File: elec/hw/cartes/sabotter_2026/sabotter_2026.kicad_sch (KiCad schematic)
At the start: 0 parts

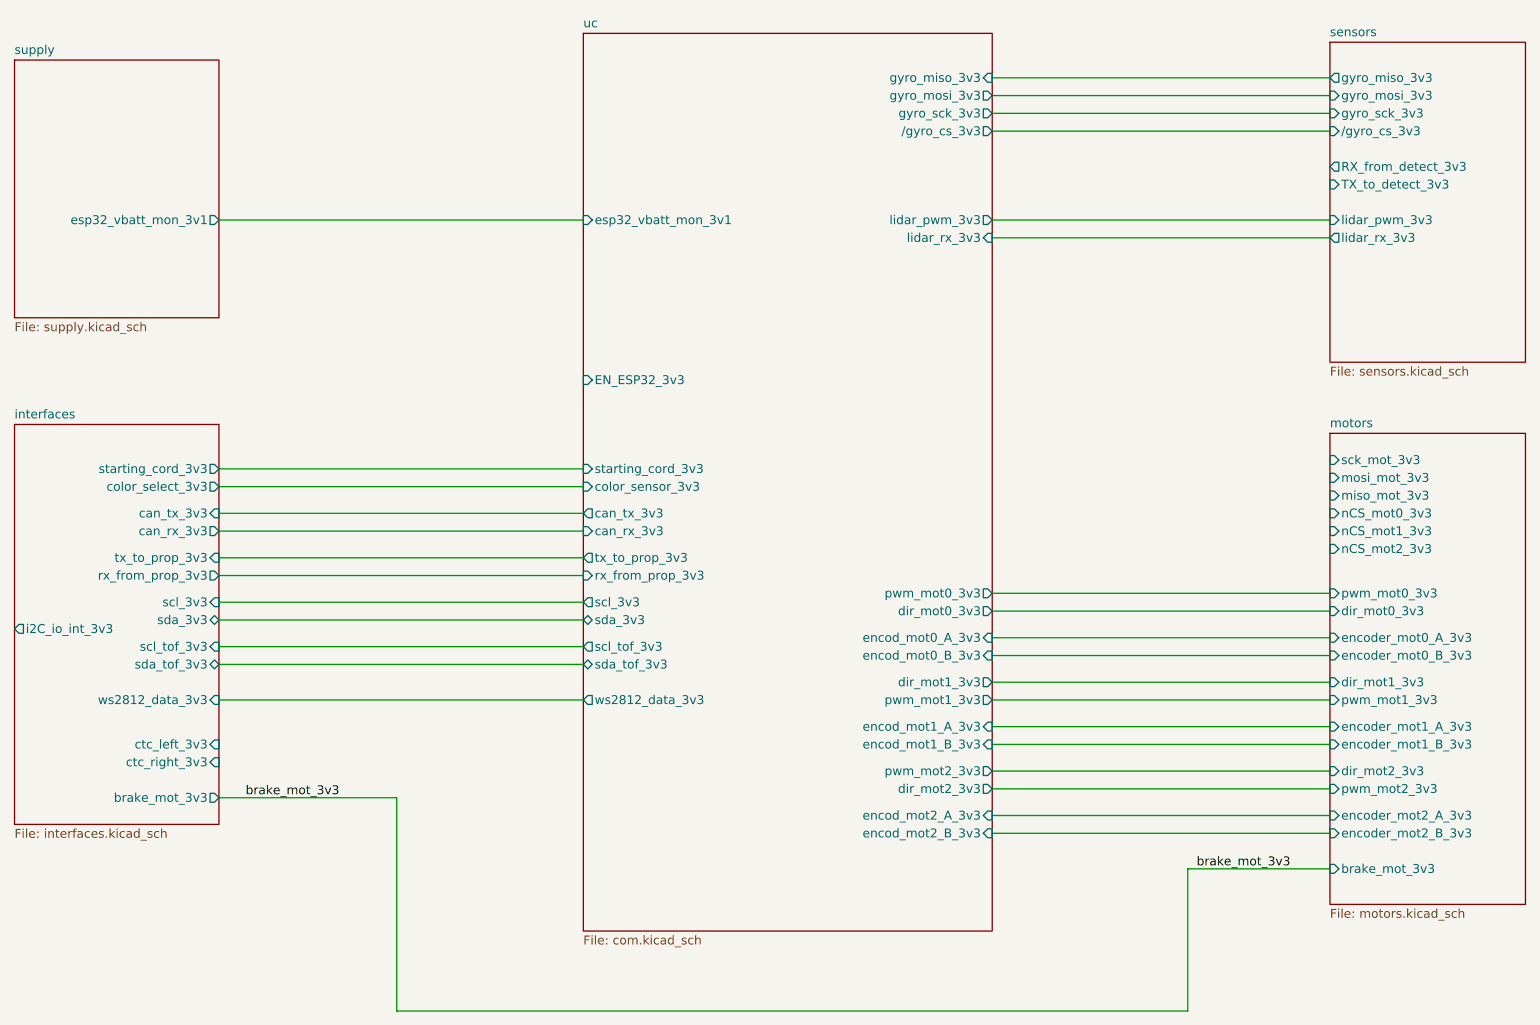
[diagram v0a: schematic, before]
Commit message: switchs added to motor ribbon cable
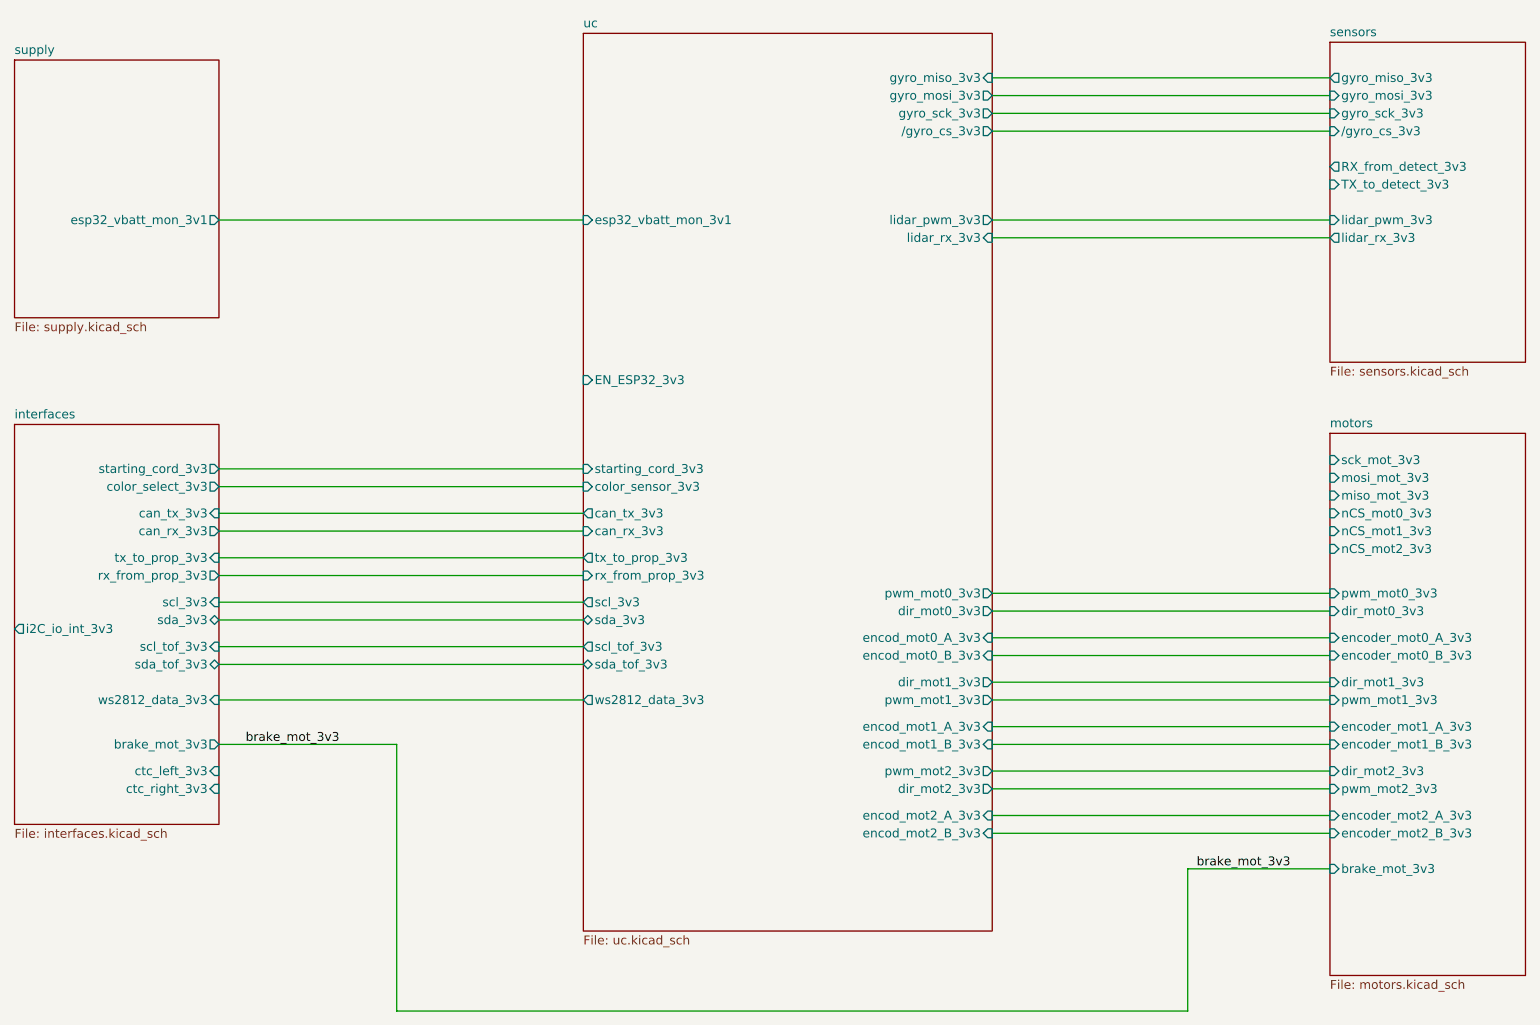
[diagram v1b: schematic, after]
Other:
- sheet uc: file com.kicad_sch -> uc.kicad_sch
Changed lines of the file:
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@@
 	(wire
 		(pts
-			(xy 58.42 130.81) (xy 83.82 130.81)
+			(xy 58.42 123.19) (xy 83.82 123.19)
 		)
 		(stroke
@@
 	(wire
 		(pts
-			(xy 83.82 130.81) (xy 83.82 161.29)
+			(xy 83.82 123.19) (xy 83.82 161.29)
 		)
 		(stroke
@@
 	)
 	(label "brake_mot_3v3"
-		(at 62.23 130.81 0)
+		(at 62.23 123.19 0)
 		(effects
 			(font
@@
 			)
 		)
-		(property "Sheetfile" "com.kicad_sch"
+		(property "Sheetfile" "uc.kicad_sch"
 			(at 110.49 150.4446 0)
 			(effects
@@
 	(sheet
 		(at 217.17 78.74)
-		(size 27.94 67.31)
+		(size 27.94 77.47)
 		(fields_autoplaced yes)
 		(stroke
@@
 		)
 		(property "Sheetfile" "motors.kicad_sch"
-			(at 217.17 146.6346 0)
+			(at 217.17 156.7946 0)
 			(effects
 				(font
@@
 			)
 		)
-		(pin "ctc_left_3v3" input
-			(at 58.42 123.19 0)
-			(effects
-				(font
-					(size 1.27 1.27)
-				)
-				(justify right)
-			)
-		)
-		(pin "ctc_right_3v3" input
-			(at 58.42 125.73 0)
-			(effects
-				(font
-					(size 1.27 1.27)
-				)
-				(justify right)
-			)
-		)
 		(pin "i2C_io_int_3v3" output
 			(at 29.21 106.68 180)
@@
 		)
 		(pin "brake_mot_3v3" output
-			(at 58.42 130.81 0)
-			(effects
-				(font
+			(at 58.42 123.19 0)
+			(effects
+				(font
+					(size 1.27 1.27)
+				)
+				(justify right)
+			)
+		)
+		(pin "ctc_left_3v3" input
+			(at 58.42 127 0)
+			(effects
+				(font
+					(size 1.27 1.27)
+				)
+				(justify right)
+			)
+		)
+		(pin "ctc_right_3v3" input
+			(at 58.42 129.54 0)
+			(effects
+				(font

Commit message: sabotter wip
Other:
- sheet motors ports: added irq0_3v3, irq1_3v3, scl_tof_3v3, sda_tof_3v3; removed miso_mot_3v3, mosi_mot_3v3, nCS_mot0_3v3, nCS_mot1_3v3, nCS_mot2_3v3, sck_mot_3v3
- sheet uc ports: added none; removed EN_ESP32_3v3
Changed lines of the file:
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@@
+	(wire
+		(pts
+			(xy 199.39 90.17) (xy 217.17 90.17)
+		)
+		(stroke
+			(width 0)
+			(type default)
+		)
+	)
 	(wire
 		(pts
@@
 	(wire
 		(pts
+			(xy 199.39 92.71) (xy 217.17 92.71)
+		)
+		(stroke
+			(width 0)
+			(type default)
+		)
+	)
+	(wire
+		(pts
 			(xy 168.91 133.35) (xy 217.17 133.35)
 		)
@@
 			(width 0)
 			(type default)
+		)
+	)
+	(label "scl_tof_3v3"
+		(at 199.39 90.17 0)
+		(effects
+			(font
+				(size 1.27 1.27)
+			)
+			(justify left bottom)
 		)
 	)
@@
 		)
 	)
+	(label "sda_tof_3v3"
+		(at 199.39 92.71 0)
+		(effects
+			(font
+				(size 1.27 1.27)
+			)
+			(justify left bottom)
+		)
+	)
+	(label "scl_tof_3v3"
+		(at 80.01 109.22 0)
+		(effects
+			(font
+				(size 1.27 1.27)
+			)
+			(justify left bottom)
+		)
+	)
 	(label "brake_mot_3v3"
 		(at 198.12 140.97 0)
@@
 		)
 	)
+	(label "sda_tof_3v3"
+		(at 80.01 111.76 0)
+		(effects
+			(font
+				(size 1.27 1.27)
+			)
+			(justify left bottom)
+		)
+	)
 	(sheet
 		(at 110.49 21.59)
@@
 			)
 		)
-		(pin "EN_ESP32_3v3" input
-			(at 110.49 71.12 180)
-			(effects
-				(font
-					(size 1.27 1.27)
-				)
-				(justify left)
-			)
-		)
 		(pin "color_sensor_3v3" input
 			(at 110.49 86.36 180)
@@
 			)
 		)
-		(pin "sck_mot_3v3" input
-			(at 217.17 82.55 180)
-			(effects
-				(font
-					(size 1.27 1.27)
-				)
-				(justify left)
-			)
-		)
-		(pin "mosi_mot_3v3" input
-			(at 217.17 85.09 180)
-			(effects
-				(font
-					(size 1.27 1.27)
-				)
-				(justify left)
-			)
-		)
-		(pin "miso_mot_3v3" input
-			(at 217.17 87.63 180)
-			(effects
-				(font
-					(size 1.27 1.27)
-				)
-				(justify left)
-			)
-		)
-		(pin "nCS_mot2_3v3" input
-			(at 217.17 95.25 180)
-			(effects
-				(font
-					(size 1.27 1.27)
-				)
-				(justify left)
-			)
-		)
 		(pin "pwm_mot2_3v3" input
 			(at 217.17 129.54 180)
@@
 			)
 		)
-		(pin "nCS_mot1_3v3" input
-			(at 217.17 92.71 180)
-			(effects
-				(font
-					(size 1.27 1.27)
-				)
-				(justify left)
-			)
-		)
-		(pin "nCS_mot0_3v3" input
-			(at 217.17 90.17 180)
-			(effects
-				(font
-					(size 1.27 1.27)
-				)
-				(justify left)
-			)
-		)
 		(pin "dir_mot1_3v3" input
 			(at 217.17 114.3 180)
@@
 			(effects
 				(font
+					(size 1.27 1.27)
+				)
+				(justify left)
+			)
+		)
+		(pin "irq1_3v3" output
+			(at 217.17 87.63 180)
+			(effects
+				(font
+					(size 1.27 1.27)
+				)
+				(justify left)
+			)
+		)
+		(pin "irq0_3v3" output
+			(at 217.17 85.09 180)
+			(effects
+				(font
+					(size 1.27 1.27)
+				)
+				(justify left)
+			)
+		)
+		(pin "sda_tof_3v3" bidirectional
+			(at 217.17 92.71 180)
+			(effects
+				(font
+					(size 1.27 1.27)
+				)
+				(justify left)
+			)
+		)
+		(pin "scl_tof_3v3" input
+			(at 217.17 90.17 180)
+			(effects
+				(font

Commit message: sabotter wip
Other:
- sheet sensors ports: added none; removed RX_from_detect_3v3, TX_to_detect_3v3
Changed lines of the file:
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@@
-			)
-		)
-		(pin "RX_from_detect_3v3" output
-			(at 217.17 40.64 180)
-			(effects
-				(font
-					(size 1.27 1.27)
-				)
-				(justify left)
-			)
-		)
-		(pin "TX_to_detect_3v3" input
-			(at 217.17 43.18 180)
-			(effects
-				(font
-					(size 1.27 1.27)
-				)
-				(justify left)
 			)
 		)

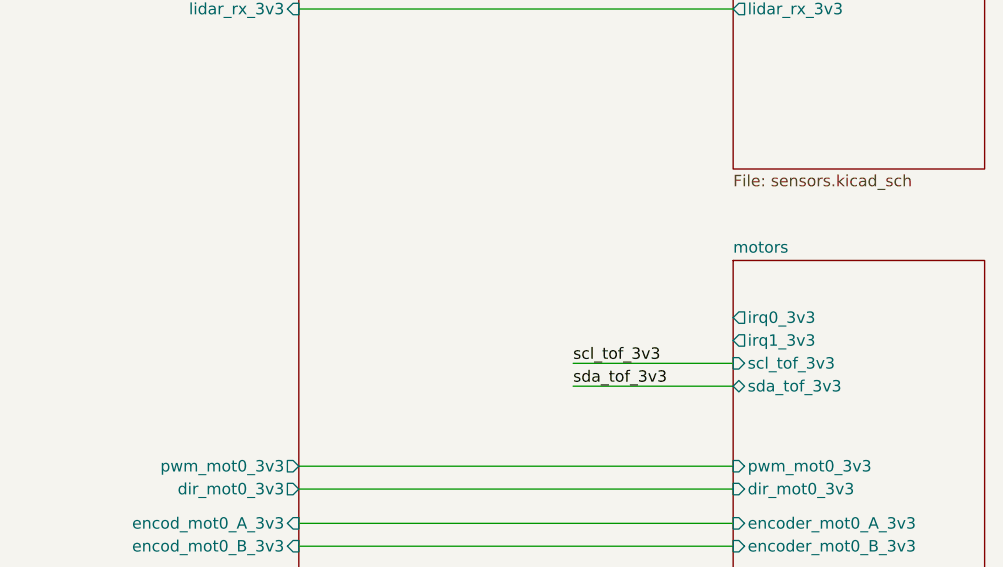
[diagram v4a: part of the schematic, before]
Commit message: tof irq added, needs routing
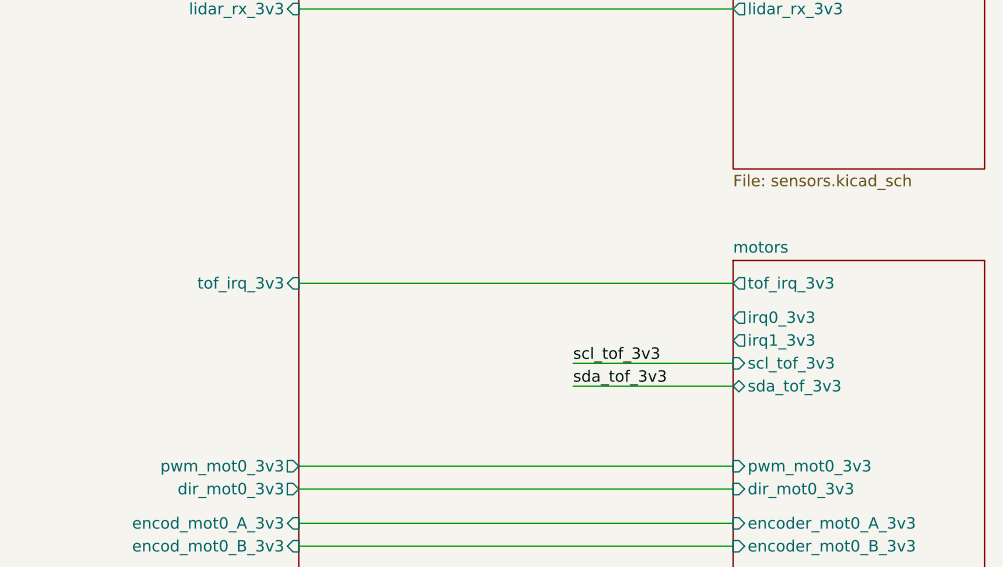
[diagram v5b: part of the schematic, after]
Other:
- sheet motors ports: added tof_irq_3v3; removed none
- sheet uc ports: added tof_irq_3v3; removed none
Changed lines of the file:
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@@
+	(wire
+		(pts
+			(xy 168.91 81.28) (xy 217.17 81.28)
+		)
+		(stroke
+			(width 0)
+			(type default)
+		)
+	)
 	(wire
 		(pts
@@
 			)
 		)
+		(pin "tof_irq_3v3" input
+			(at 168.91 81.28 0)
+			(effects
+				(font
+					(size 1.27 1.27)
+				)
+				(justify right)
+			)
+		)
 		(instances
 			(project "sabotter_2026"
@@
 			(effects
 				(font
+					(size 1.27 1.27)
+				)
+				(justify left)
+			)
+		)
+		(pin "tof_irq_3v3" output
+			(at 217.17 81.28 180)
+			(effects
+				(font

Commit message: sabotter corrected after review
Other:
- sheet interfaces ports: added none; removed color_select_3v3, ctc_left_3v3, ctc_right_3v3, i2C_io_int_3v3, starting_cord_3v3
- sheet motors ports: added none; removed irq0_3v3, irq1_3v3
- sheet uc ports: added none; removed color_sensor_3v3, starting_cord_3v3
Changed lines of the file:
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@@
-	(wire
-		(pts
-			(xy 58.42 83.82) (xy 110.49 83.82)
-		)
-		(stroke
-			(width 0)
-			(type default)
-		)
-	)
 	(wire
 		(pts
@@
 		(pts
 			(xy 168.91 127) (xy 217.17 127)
-		)
-		(stroke
-			(width 0)
-			(type default)
-		)
-	)
-	(wire
-		(pts
-			(xy 58.42 81.28) (xy 110.49 81.28)
 		)
 		(stroke
@@
 			)
 		)
-		(pin "color_sensor_3v3" input
-			(at 110.49 83.82 180)
-			(effects
-				(font
-					(size 1.27 1.27)
-				)
-				(justify left)
-			)
-		)
 		(pin "encod_mot2_A_3v3" input
 			(at 168.91 133.35 0)
@@
 				)
 				(justify right)
-			)
-		)
-		(pin "starting_cord_3v3" input
-			(at 110.49 81.28 180)
-			(effects
-				(font
-					(size 1.27 1.27)
-				)
-				(justify left)
 			)
 		)
@@
 			)
 		)
-		(pin "irq0_3v3" output
-			(at 217.17 83.82 180)
-			(effects
-				(font
-					(size 1.27 1.27)
-				)
-				(justify left)
-			)
-		)
-		(pin "irq1_3v3" output
-			(at 217.17 86.36 180)
-			(effects
-				(font
-					(size 1.27 1.27)
-				)
-				(justify left)
-			)
-		)
 		(instances
 			(project "sabotter_2026"
@@
 			)
 		)
-		(pin "starting_cord_3v3" output
-			(at 58.42 81.28 0)
-			(effects
-				(font
-					(size 1.27 1.27)
-				)
-				(justify right)
-			)
-		)
-		(pin "color_select_3v3" output
-			(at 58.42 83.82 0)
-			(effects
-				(font
-					(size 1.27 1.27)
-				)
-				(justify right)
-			)
-		)
 		(pin "can_tx_3v3" input
 			(at 58.42 87.63 0)
@@
 			)
 		)
-		(pin "i2C_io_int_3v3" output
-			(at 58.42 100.33 0)
-			(effects
-				(font
-					(size 1.27 1.27)
-				)
-				(justify right)
-			)
-		)
 		(pin "brake_mot_3v3" output
 			(at 58.42 123.19 0)
 			(effects
 				(font
-					(size 1.27 1.27)
-				)
-				(justify right)
-			)
-		)
-		(pin "ctc_left_3v3" input
-			(at 58.42 127 0)
-			(effects
-				(font
-					(size 1.27 1.27)
-				)
-				(justify right)
-			)
-		)
-		(pin "ctc_right_3v3" input
-			(at 58.42 129.54 0)
-			(effects
-				(font
